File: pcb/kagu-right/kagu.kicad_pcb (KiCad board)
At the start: 2 copper layers, 127 x 91.5 mm, 62 parts, among them SW1 SW_Push, SW10 SW_Push, SW11 SW_Push, SW12 SW_Push, SW13 SW_Push, SW14 SW_Push, SW15 SW_Push, SW16 SW_Push, SW17 SW_Push, SW18 SW_Push, SW19 SW_Push, SW2 SW_Push, SW3 SW_Push, SW4 SW_Push, SW5 SW_Push, SW6 SW_Push, SW7 SW_Push, SW8 SW_Push, SW9 SW_Push, U1 XIAO-nRF52840-Plus-SMD

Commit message: feat(pcb/ritght): update it
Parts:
- removed H3, H7: MountingHole, MountingHole:MountingHole_3.2mm_M3_DIN965_Pad
- moved H6 3.00 mm to (189.0, 61.5)
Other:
- outline, holes or cut-outs redrawn

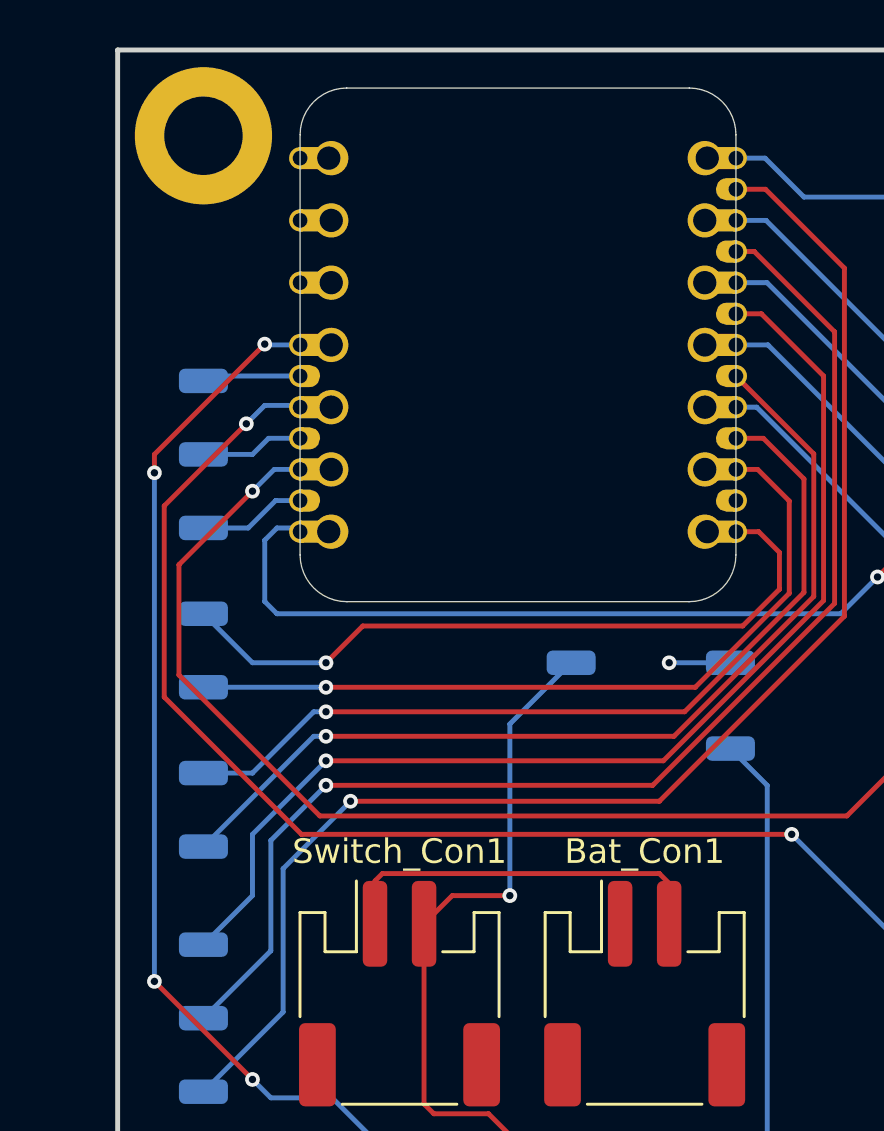
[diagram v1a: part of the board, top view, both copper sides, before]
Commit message: feat(pcb): match both sides
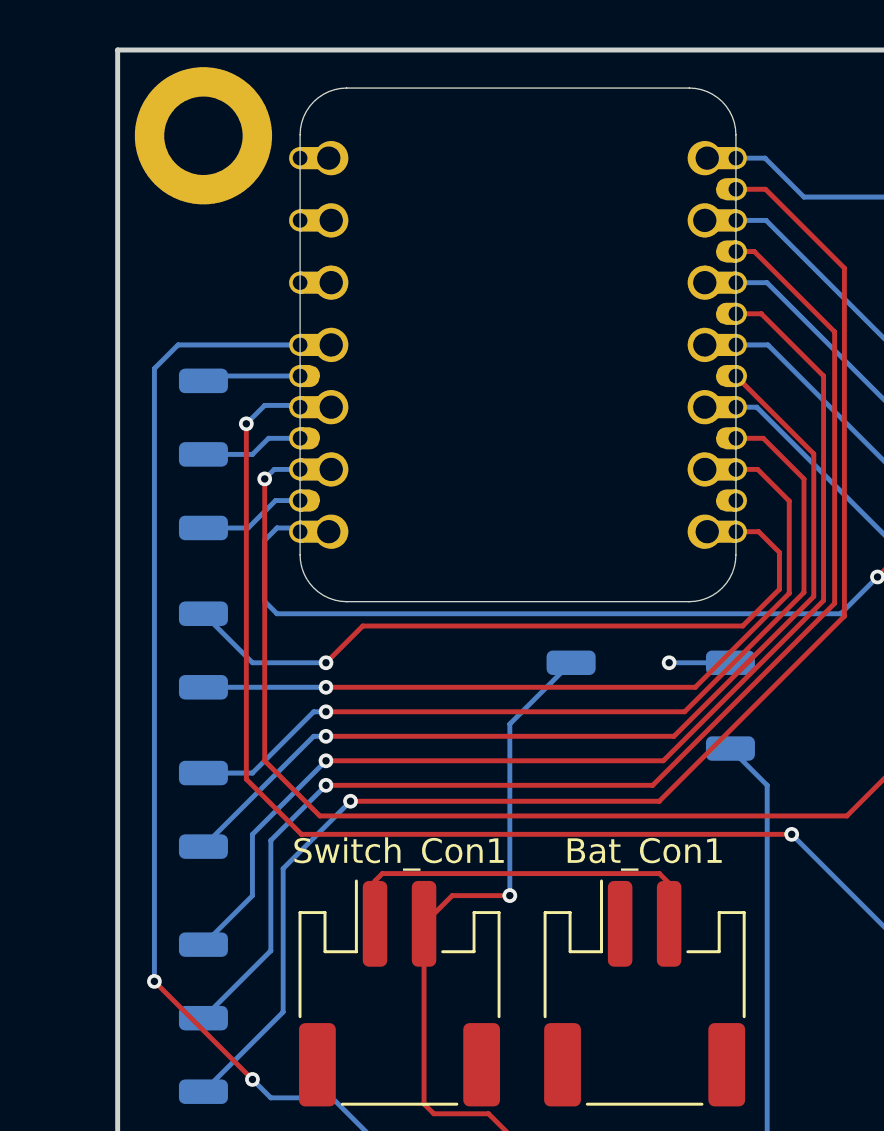
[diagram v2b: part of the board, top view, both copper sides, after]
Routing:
- net row2: track 159.1 -> 156.2 mm
- net row3: track 162.4 -> 159.6 mm
- net row4: track 99.8 -> 101.8 mm, vias 6 -> 4
